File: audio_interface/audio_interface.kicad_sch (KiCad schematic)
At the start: 44 parts, among them J1 XLR3, J2 AudioJack2, U1 NE5532, U2 NE5532, U3 NE5532

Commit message: Further changes
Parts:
- added C1, C2, C9: 100p, symbol Device:C
- added C14, C8: 47n, symbol Device:C
- added C7: 10p, symbol Device:C
- added JP7, JP8: Jumper_2_Bridged, symbol Jumper:Jumper_2_Bridged
- added R1, R4: 1M, symbol Device:R_US
- added R13, R18: 100, symbol Device:R_US
- C12, C13: renamed from C?; value C -> 0.1u
- C17: renamed from C7; value 01.u -> 0.1u
- C3: renamed from C1; value 10p -> 100p
- C4: renamed from C2; value 10p -> 100p
- C5: renamed from C3; value 10p -> 100p
- C6: renamed from C4; value 10p -> 100p
- gave numbers to parts that had none: 3
- renumbered C5 to C10, C6 to C11, C8 to C18, C9 to C19, C10 to C20, R8 to R10, R9 to R11, R10 to R12, R11 to R14, R12 to R15, R13 to R16, R14 to R17, R1 to R2, R2 to R3, R3 to R5, R4 to R6, R5 to R7, R6 to R8, R7 to R9, U3 to U1, U1 to U2, U2 to U3
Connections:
- net 2V5A_I: now also JP8.2 (B); no longer U4.6 (-), U4.7
- net 2V5A_M: now also JP7.2 (B); no longer U4.1, U4.2 (-)
- net GNDA: now also C14.2, C2.2, C8.2, R4.2
- net INST_OUT: now also C8.1, R13.2; no longer R12.2, U3.1
- net MIC_OUT: now also C14.1, R18.2; no longer R17.2, U1.1
- net at JP1.2 (B), R2.1: now also C1.1, R1.1
- net at R16.1, R17.1, U1.2 (-): now also C9.1
- net at JP2.2 (B), R3.1: now also C1.2, R1.2
- net at R11.1, R12.1, U3.2 (-): now also C7.2
- net at JP3.2 (B), U2.5 (+): now also C2.1, R4.1
- new net: JP7.1 (A), U4.1, U4.2 (-)
- new net: C9.2, R17.2, R18.1, U1.1
- new net: C7.1, R12.2, R13.1, U3.1
- new net: JP8.1 (A), U4.6 (-), U4.7
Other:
- note added: "AA filter (DNP unless needed)"
- moved on the sheet: C15, C16, J2, JP1, JP2, JP3, R11, R16, R2, R3, U1B, U4A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

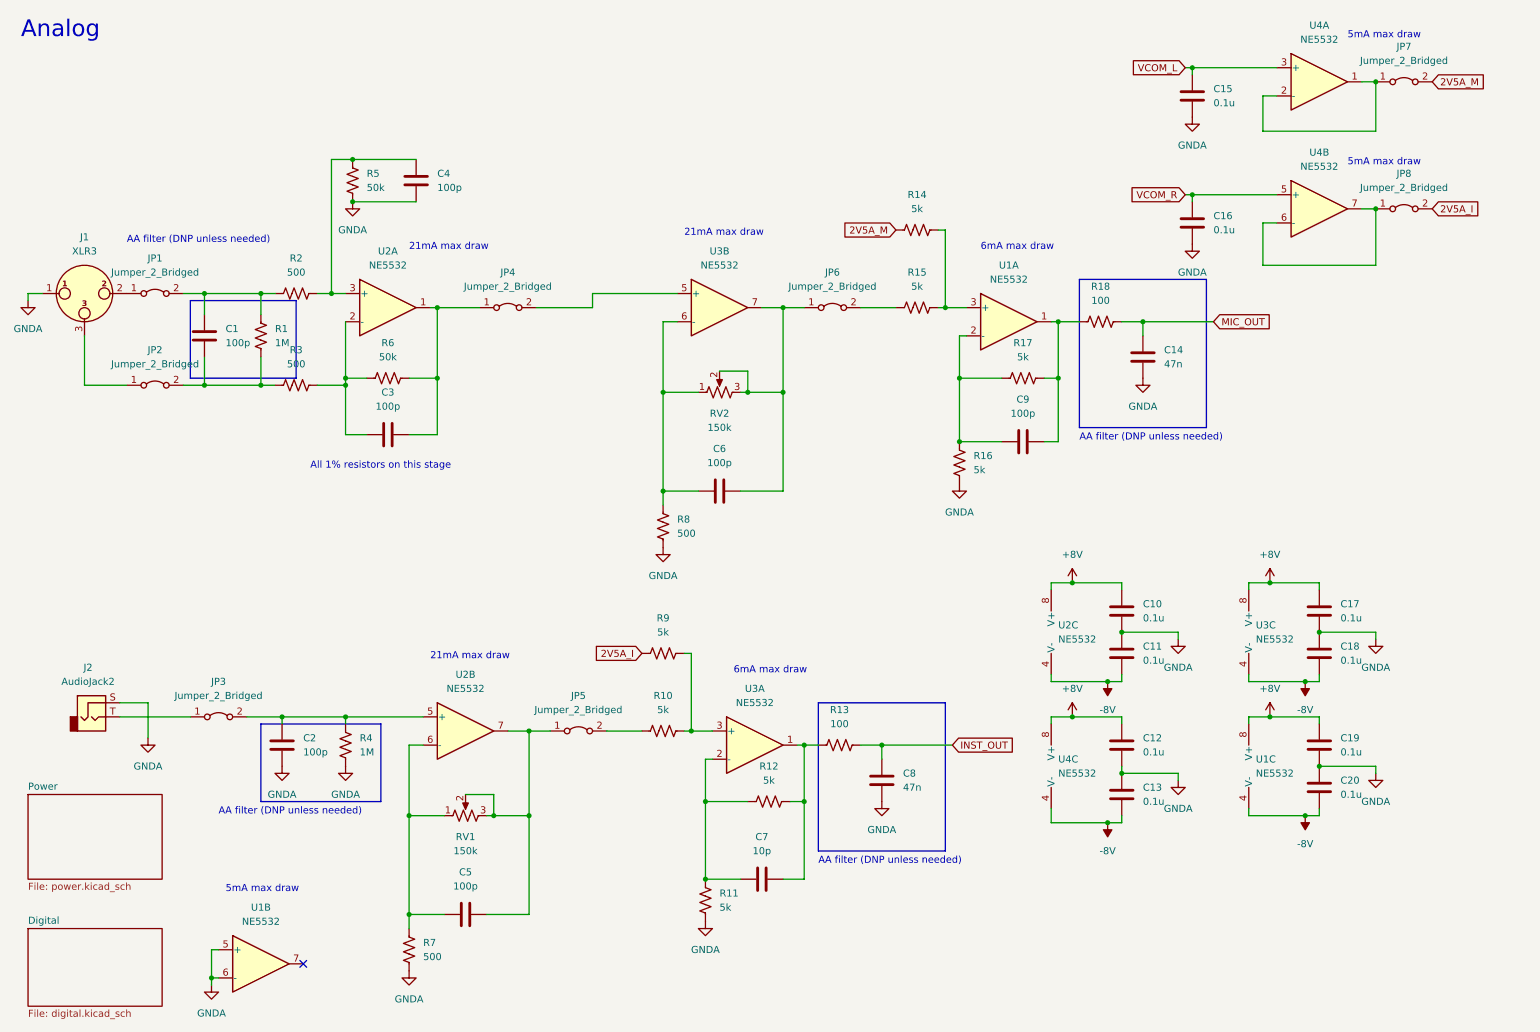
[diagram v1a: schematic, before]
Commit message: Added TP and fixed some capacitor values after SPICE sim.
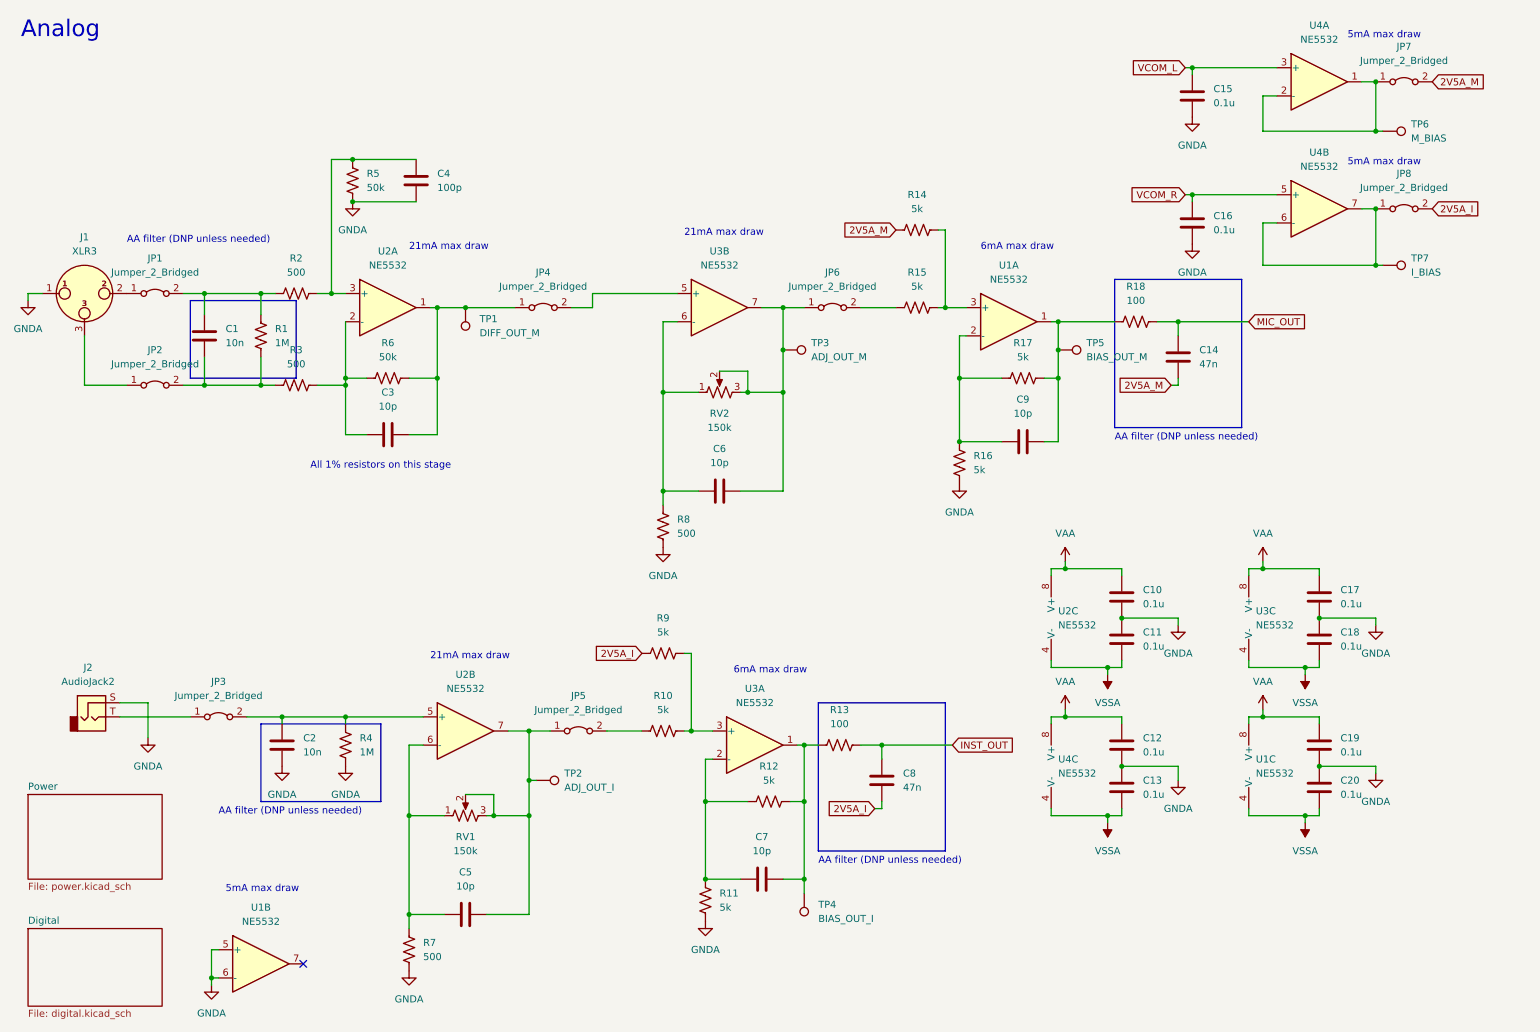
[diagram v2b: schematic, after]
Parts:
- added TP1: DIFF_OUT_M, symbol Connector:TestPoint
- added TP2: ADJ_OUT_I, symbol Connector:TestPoint
- added TP3: ADJ_OUT_M, symbol Connector:TestPoint
- added TP4: BIAS_OUT_I, symbol Connector:TestPoint
- added TP5: BIAS_OUT_M, symbol Connector:TestPoint
- added TP6: M_BIAS, symbol Connector:TestPoint
- added TP7: I_BIAS, symbol Connector:TestPoint
- C1, C2: value 100p -> 10n
- C3, C5, C6, C9: value 100p -> 10p
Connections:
- net 2V5A_I: now also C8.2
- net 2V5A_M: now also C14.2
- net GNDA: no longer C14.2, C8.2
- net at C3.2, JP4.1 (A), R6.2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: now also TP1.1
- net at JP7.1 (A), U4.1, U4.2 (-): now also TP6.1
- net at C6.1, JP6.1 (A), RV2.2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: now also TP3.1
- net at C9.2, R17.2, R18.1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: now also TP5.1
- net at C7.1, R12.2, R13.1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: now also TP4.1
- net at C5.1, JP5.1 (A), RV1.2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: now also TP2.1
- net at JP8.1 (A), U4.6 (-), U4.7: now also TP7.1
- net +8V renamed VAA
- net -8V renamed VSSA
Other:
- moved on the sheet: C10, C11, C13, C14, C17, C18, R18, U2C, U3C

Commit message: Added some footprints.
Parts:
- C1, C10, C11, C12, C13, C14, C15, C16, C17, C18, C19, C2, C20, C3, C5, C6, C7, C8, C9: footprint (none) -> Capacitor_SMD:C_0805_2012Metric_Pad1.15x1.40mm_HandSolder
- C4: value 100p -> 10p; footprint (none) -> Capacitor_SMD:C_0805_2012Metric_Pad1.15x1.40mm_HandSolder
- JP1, JP2, JP3, JP4, JP5, JP6, JP7, JP8, R1, R10, R11, R12, R13, R14, R15, R16, R17, R18, R2, R3, R4, R5, R6, R7, R8, R9: footprint (none) -> Resistor_SMD:R_1206_3216Metric_Pad1.42x1.75mm_HandSolder
- TP1, TP2, TP3, TP4, TP5, TP6, TP7: footprint (none) -> TestPoint:TestPoint_Loop_D2.54mm_Drill1.5mm_Beaded
- U1, U2, U3, U4: footprint (none) -> Package_DIP:DIP-8_W7.62mm_Socket

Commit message: Finished footprints.
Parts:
- removed C14, C8: 47n, Capacitor_SMD:C_0805_2012Metric_Pad1.15x1.40mm_HandSolder, symbol Device:C
- removed R13, R18: 100, Resistor_SMD:R_1206_3216Metric_Pad1.42x1.75mm_HandSolder, symbol Device:R_US
- C1, C10, C11, C12, C13, C15, C16, C17, C18, C19, C2, C20, C3, C4, C5, C6, C7, C9: footprint Capacitor_SMD:C_0805_2012Metric_Pad1.15x1.40mm_HandSolder -> Capacitor_SMD:C_0805_2012Metric_Pad1.18x1.45mm_HandSolder
- J1: footprint (none) -> Connector_Audio:Jack_XLR_Neutrik_NC3FAAH-0_Horizontal
- J2: footprint (none) -> Connector_Audio:Jack_6.35mm_Neutrik_NMJ4HFD3_Horizontal
- JP1, JP2, JP3, JP4, JP5, JP6, JP7, JP8, R1, R10, R11, R12, R14, R15, R16, R17, R2, R3, R4, R5, R6, R7, R8, R9: footprint Resistor_SMD:R_1206_3216Metric_Pad1.42x1.75mm_HandSolder -> Resistor_SMD:R_1206_3216Metric_Pad1.30x1.75mm_HandSolder
- RV1, RV2: footprint (none) -> Library:PDB181-K420F-103A2
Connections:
- net INST_OUT: now also C7.1, R12.2, TP4.1, U3.1
- net MIC_OUT: now also C9.2, R17.2, TP5.1, U1.1

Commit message: Orion's layout
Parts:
- removed U1, U2, U3, U4: NE5532, Package_DIP:DIP-8_W7.62mm_Socket, symbol Amplifier_Operational:NE5532
- added U1, U2, U3, U4: (no value), symbol Amplifier_Operational:OPA2134
- TP6: value M_BIAS -> (none)
- TP7: value I_BIAS -> (none)
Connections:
- net 2V5A_I: now also JP7.2 (B); no longer JP8.2 (B)
- net 2V5A_M: now also JP8.2 (B); no longer JP7.2 (B)
- net GNDA: now also U1.2 (-), U1.3 (+)
- net INST_OUT: now also U3.1
- net MIC_OUT: now also U4.1
- net VAA: now also U1.8 (V+), U2.8 (V+), U3.8 (V+), U4.8 (V+)
- net VCOM_L: now also C16.1, U4.5 (+); no longer C15.1
- net VCOM_R: now also C15.1, U3.5 (+); no longer C16.1
- net VSSA: now also U1.4 (V-), U2.4 (V-), U3.4 (V-), U4.4 (V-)
- net at C3.1, R3.2, R6.1: now also U2.2 (-)
- net at C3.2, JP4.1 (A), R6.2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: now also U2.1
- net at C6.1, JP6.1 (A), RV2.2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: now also U2.7
- net at JP7.1 (A), TP6.1: now also U3.6 (-), U3.7
- net at C6.2, R8.1, RV2.1: now also U2.6 (-)
- net at R14.2, R15.2: now also U4.3 (+)
- net at C2.1, JP3.2 (B), R4.1: now also U1.5 (+)
- net at C5.1, JP5.1 (A), RV1.2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: now also U1.7
- net at C9.1, R16.1, R17.1: now also U4.2 (-)
- net at JP4.2 (B): now also U2.5 (+)
- net at C7.2, R11.1, R12.1: now also U3.2 (-)
- net at C4.1, R2.2, R5.1: now also U2.3 (+)
- net at C5.2, R7.1, RV1.1: now also U1.6 (-)
- net at R10.2, R9.2: now also U3.3 (+)
- net at JP8.1 (A), TP7.1: now also U4.6 (-), U4.7

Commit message: Fixed some layout issues. Flipped ADC.
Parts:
- TP6: value (none) -> I_BIAS
- TP7: value (none) -> M_BIAS
- U1, U2, U3, U4: value (none) -> OPA2134; footprint (none) -> Package_DIP:DIP-8_W7.62mm_Socket
- U1: footprint (none) -> Package_DIP:DIP-8_W7.62mm_Socket
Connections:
- net VCOM_L: now also C15.1, U3.5 (+); no longer C16.1, U4.5 (+)
- net VCOM_R: now also C16.1, U4.5 (+); no longer C15.1, U3.5 (+)
